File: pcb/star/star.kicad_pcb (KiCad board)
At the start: 2 copper layers, 49.1 x 46.7 mm, 19 parts, among them U1 AP2112K-3.3, U2 74AHC595, U3 74AHC595

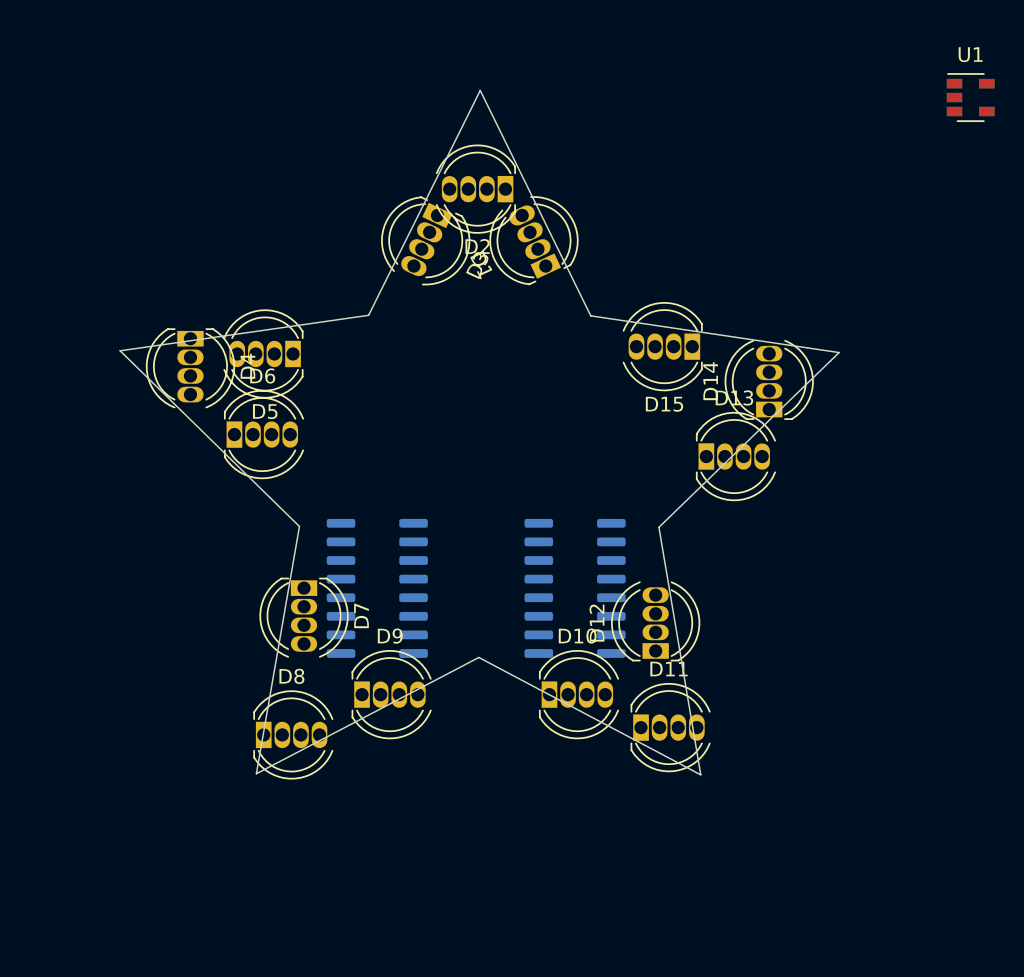
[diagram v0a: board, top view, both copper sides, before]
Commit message: outline increased
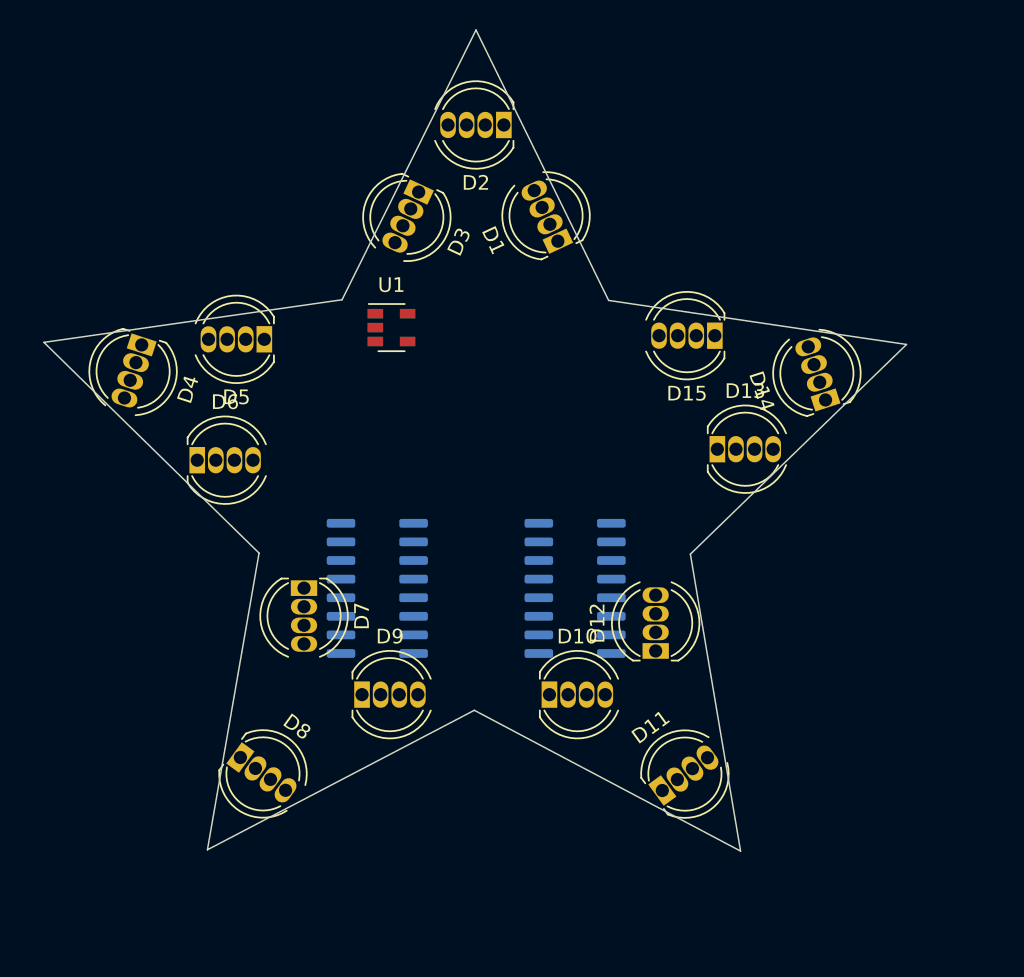
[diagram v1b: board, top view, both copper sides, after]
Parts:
- moved U1 42.5 mm to (92.2, 75.2)
- moved D11 4.53 mm to (110.7, 106.8), turned to 36 degrees
- moved D2 4.38 mm to (99.9, 61.4)
- moved D14 3.90 mm to (121.8, 80.1), turned to 108 degrees
- moved D4 3.35 mm to (75.2, 76.4), turned to 252 degrees
- moved D6 3.08 mm to (79.0, 84.2)
- moved D8 2.22 mm to (81.9, 104.5), turned to 324 degrees
- moved D5 2.20 mm to (83.5, 76.0)
- moved D3 2.05 mm to (94.1, 65.9)
- moved D1 1.89 mm to (103.6, 69.3)
- moved D15 1.71 mm to (114.3, 75.8)
- moved D13 0.90 mm to (114.5, 83.5)
- moved G*** 0.83 mm to (97.9, 83.2)
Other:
- board size 49.1 x 46.7 mm -> 58.9 x 56 mm

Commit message: apa106 and esp12f used
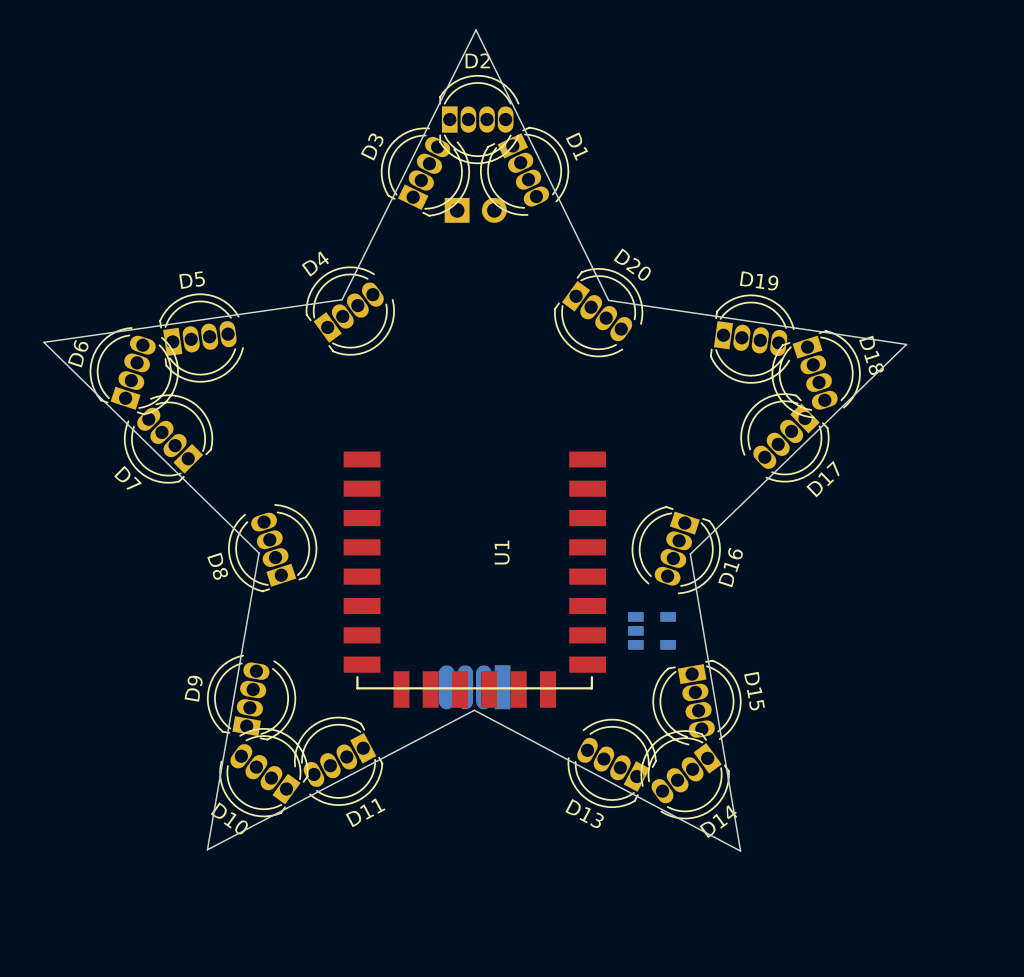
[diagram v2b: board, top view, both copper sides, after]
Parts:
- removed the U2 at (91.2, 93.0)
- removed U3: 74AHC595, Package_SO:SOIC-16_3.9x9.9mm_P1.27mm
- added D16: APA-106-F5, LED_THT:LED_D5.0mm-4_RGB, F.Cu at (112.2, 88.5)
- added D17: APA-106-F5, LED_THT:LED_D5.0mm-4_RGB, F.Cu at (120.4, 81.4)
- added D18: APA-106-F5, LED_THT:LED_D5.0mm-4_RGB, F.Cu at (120.6, 76.5)
- added D19: APA-106-F5, LED_THT:LED_D5.0mm-4_RGB, F.Cu at (114.9, 75.7)
- added D20: APA-106-F5, LED_THT:LED_D5.0mm-4_RGB, F.Cu at (104.8, 73.1)
- added J1: POWER, Connector_PinSocket_2.54mm:PinSocket_1x02_P2.54mm_Vertical, B.Cu at (96.7, 67.2)
- added U1: ESP-12F, ESP8266:ESP-12E_SMD, F.Cu at (90.9, 84.2)
- D1, D10, D11, D13, D14, D15, D2, D3, D4, D5, D6, D7, D8, D9: value LED_RGBC -> APA-106-F5
- D12: value LED_RGBC -> APA-106-F5; moved to B.Cu
- U2: renamed from U1; moved to B.Cu
- moved U2 27.3 mm to (110.0, 95.9)
- moved D14 25.8 mm to (113.8, 104.6), turned to 216 degrees
- moved D15 23.1 mm to (112.7, 98.8), turned to 280 degrees
- moved D13 23.0 mm to (109.0, 105.8), turned to 152 degrees
- moved D11 20.6 mm to (90.3, 103.9), turned to 208 degrees
- moved D10 19.1 mm to (85.1, 106.7), turned to 144 degrees
- moved D4 12.8 mm to (87.9, 75.2), turned to 36 degrees
- moved D8 12.8 mm to (84.7, 92.1), turned to 108 degrees
- moved D7 11.8 mm to (78.3, 84.2), turned to 135 degrees
- moved D12 10.7 mm to (99.8, 99.8), turned to 180 degrees
- moved D9 8.16 mm to (82.3, 102.4), turned to 80 degrees
- moved D1 7.19 mm to (100.5, 62.8), turned to 295 degrees
- moved D6 6.46 mm to (74.1, 80.0), turned to 72 degrees
- moved D5 6.25 mm to (77.3, 76.2), turned to 8 degrees
- moved D2 3.71 mm to (96.2, 61.0), turned to 0 degrees
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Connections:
- D1 pad 2: Net-(D1-Pad2) -> GND
- D1 pad 3: Net-(D1-Pad3) -> +5V
- D10 pad 1: Net-(D10-Pad1) -> /DoD10
- D10 pad 2: Net-(D10-Pad2) -> GND
- D10 pad 3: Net-(D10-Pad3) -> +5V
- D11 pad 2: Net-(D11-Pad2) -> GND
- D11 pad 3: Net-(D11-Pad3) -> +5V
- D11 pad 4: Net-(D11-Pad4) -> /DoD10
- D12 pad 2: Net-(D12-Pad2) -> GND
- D12 pad 3: Net-(D12-Pad3) -> +5V
- D12 pad 4: Net-(D12-Pad4) -> Net-(D11-Pad1)
- D13 pad 2: Net-(D13-Pad2) -> GND
- D13 pad 3: Net-(D13-Pad3) -> +5V
- D13 pad 4: Net-(D13-Pad4) -> Net-(D12-Pad1)
- D14 pad 2: Net-(D14-Pad2) -> GND
- D14 pad 3: Net-(D14-Pad3) -> +5V
- D14 pad 4: Net-(D14-Pad4) -> Net-(D13-Pad1)
- D15 pad 1: Net-(D15-Pad1) -> /DoD15
- D15 pad 2: Net-(D15-Pad2) -> GND
- D15 pad 3: Net-(D15-Pad3) -> +5V
- D15 pad 4: Net-(D15-Pad4) -> Net-(D14-Pad1)
- D2 pad 2: Net-(D2-Pad2) -> GND
- D2 pad 3: Net-(D2-Pad3) -> +5V
- D2 pad 4: Net-(D2-Pad4) -> Net-(D1-Pad1)
- D3 pad 2: Net-(D3-Pad2) -> GND
- D3 pad 3: Net-(D3-Pad3) -> +5V
- D3 pad 4: Net-(D3-Pad4) -> Net-(D2-Pad1)
- D4 pad 2: Net-(D4-Pad2) -> GND
- D4 pad 3: Net-(D4-Pad3) -> +5V
- D4 pad 4: Net-(D4-Pad4) -> Net-(D3-Pad1)
- D5 pad 1: Net-(D5-Pad1) -> /DoD5
- D5 pad 2: Net-(D5-Pad2) -> GND
- D5 pad 3: Net-(D5-Pad3) -> +5V
- D5 pad 4: Net-(D5-Pad4) -> Net-(D4-Pad1)
- D6 pad 2: Net-(D6-Pad2) -> GND
- D6 pad 3: Net-(D6-Pad3) -> +5V
- D6 pad 4: Net-(D6-Pad4) -> /DoD5
- D7 pad 2: Net-(D7-Pad2) -> GND
- D7 pad 3: Net-(D7-Pad3) -> +5V
- D7 pad 4: Net-(D7-Pad4) -> Net-(D6-Pad1)
- D8 pad 2: Net-(D8-Pad2) -> GND
- D8 pad 3: Net-(D8-Pad3) -> +5V
- D8 pad 4: Net-(D8-Pad4) -> Net-(D7-Pad1)
- D9 pad 1: Net-(D9-Pad1) -> Net-(D10-Pad4)
- D9 pad 2: Net-(D9-Pad2) -> GND
- D9 pad 3: Net-(D9-Pad3) -> +5V
- D9 pad 4: Net-(D9-Pad4) -> Net-(D8-Pad1)
- U2 pad 1: VCC -> +5V
- U2 pad 3: VCC -> +5V

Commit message: layout first pass done
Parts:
- added C1: 10uF, Capacitor_THT:CP_Radial_D5.0mm_P2.50mm, F.Cu at (96.0, 71.0)
- added C2: 1uF, Capacitor_THT:CP_Radial_D5.0mm_P2.50mm, F.Cu at (116.0, 81.3)
- added C3: 100nF, Capacitor_THT:C_Disc_D5.0mm_W2.5mm_P2.50mm, F.Cu at (100.6, 71.0)
- added C4: 100nF, Capacitor_THT:C_Disc_D5.0mm_W2.5mm_P2.50mm, B.Cu at (88.5, 102.0)
- added C5: 100nF, Capacitor_THT:C_Disc_D5.0mm_W2.5mm_P2.50mm, B.Cu at (105.5, 102.0)
- added J2: Conn_01x06_Male, star:conn_01x06_SMD, B.Cu at (98.2, 92.0)
- added R1: 10k, Resistor_THT:R_Axial_DIN0204_L3.6mm_D1.6mm_P7.62mm_Horizontal, F.Cu at (81.6, 86.0)
- added R2: 10k, Resistor_THT:R_Axial_DIN0204_L3.6mm_D1.6mm_P7.62mm_Horizontal, F.Cu at (83.9, 86.0)
- added R3: 10k, Resistor_THT:R_Axial_DIN0204_L3.6mm_D1.6mm_P7.62mm_Horizontal, F.Cu at (112.0, 86.0)
- added REF**: MountingHole_2.2mm_M2, MountingHole:MountingHole_2.2mm_M2, F.Cu at (97.9, 63.7)
- added SW1: RST, Button_Switch_SMD:SW_SPST_EVQPE1, F.Cu at (86.5, 96.5)
- added SW2: PRG, Button_Switch_SMD:SW_SPST_EVQPE1, F.Cu at (109.3, 96.5)
- moved U2 6.40 mm to (103.6, 96.0)
- moved D1 0.36 mm to (100.7, 63.1), turned to 296 degrees
- moved D3 0.33 mm to (93.5, 66.6)
- moved D2 0.32 mm to (96.1, 61.3)
- moved J1 0.30 mm to (96.7, 67.5)
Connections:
- net Net-(U1-Pad2) renamed /ADC
- D20 pad 1: Net-(D20-Pad1) -> Net-(D1-Pad4)
- D20 pad 4: Net-(D19-Pad1) -> /LED_Din
- U1 pad 1: Net-(U1-Pad1) -> /RST
- U1 pad 12: Net-(U1-Pad12) -> /GPIO0
- U1 pad 14: Net-(U1-Pad14) -> /LED_Din
- U1 pad 15: Net-(U1-Pad15) -> /RXD
- U1 pad 16: Net-(U1-Pad16) -> /TXD
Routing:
- net +5V: track 0.00 -> 197.9 mm, vias 0 -> 1
- net GND: track 0.00 -> 62.0 mm, vias 0 -> 43
- net +3V3: track 0.00 -> 53.7 mm, vias 0 -> 3
- net /RST: track 0.00 -> 45.6 mm, vias 0 -> 1
- net /GPIO0: track 0.00 -> 34.0 mm, vias 0 -> 1
- net /LED_Din: track 0.00 -> 14.8 mm
- net Net-(R1-Pad2): track 0.00 -> 14.3 mm
- net /TXD: track 0.00 -> 13.7 mm, vias 0 -> 1
- net /RXD: track 0.00 -> 10.4 mm, vias 0 -> 1
- net Net-(D12-Pad1): track 0.00 -> 8.09 mm
- net /DoD15: track 0.00 -> 7.89 mm
- net Net-(D1-Pad4): track 0.00 -> 7.55 mm
- net Net-(D3-Pad1): track 0.00 -> 7.44 mm
- net Net-(D11-Pad1): track 0.00 -> 7.42 mm
- net Net-(D16-Pad1): track 0.00 -> 7.32 mm
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- added copper zone on B.Cu, net GND
- added copper zone on F.Cu, net GND
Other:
- board size 58.9 x 56 mm -> 50.7 x 48.4 mm
- board text added: "3V3"
- board text added: "5V"
- board text added: "GND"
- board text added: "IO0"
- board text added: "RST"
- board text added: "RXD"
- board text added: "TXD"
- board text added: "jlcjlcjlcjlc"

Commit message: routing second pass
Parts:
- moved U1 1.05 mm to (90.9, 85.2)
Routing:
- net +3V3: track 53.7 -> 56.9 mm
- net /GPIO0: track 34.0 -> 32.9 mm
- net Net-(R1-Pad2): track 14.3 -> 15.4 mm
- net /LED_Din: track 14.8 -> 15.8 mm
- net /RST: track 45.6 -> 46.3 mm
- net GND: track 62.0 -> 62.7 mm, vias 43 -> 40
